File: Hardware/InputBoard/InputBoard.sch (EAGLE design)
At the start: 8 parts, among them IC1 LM358N

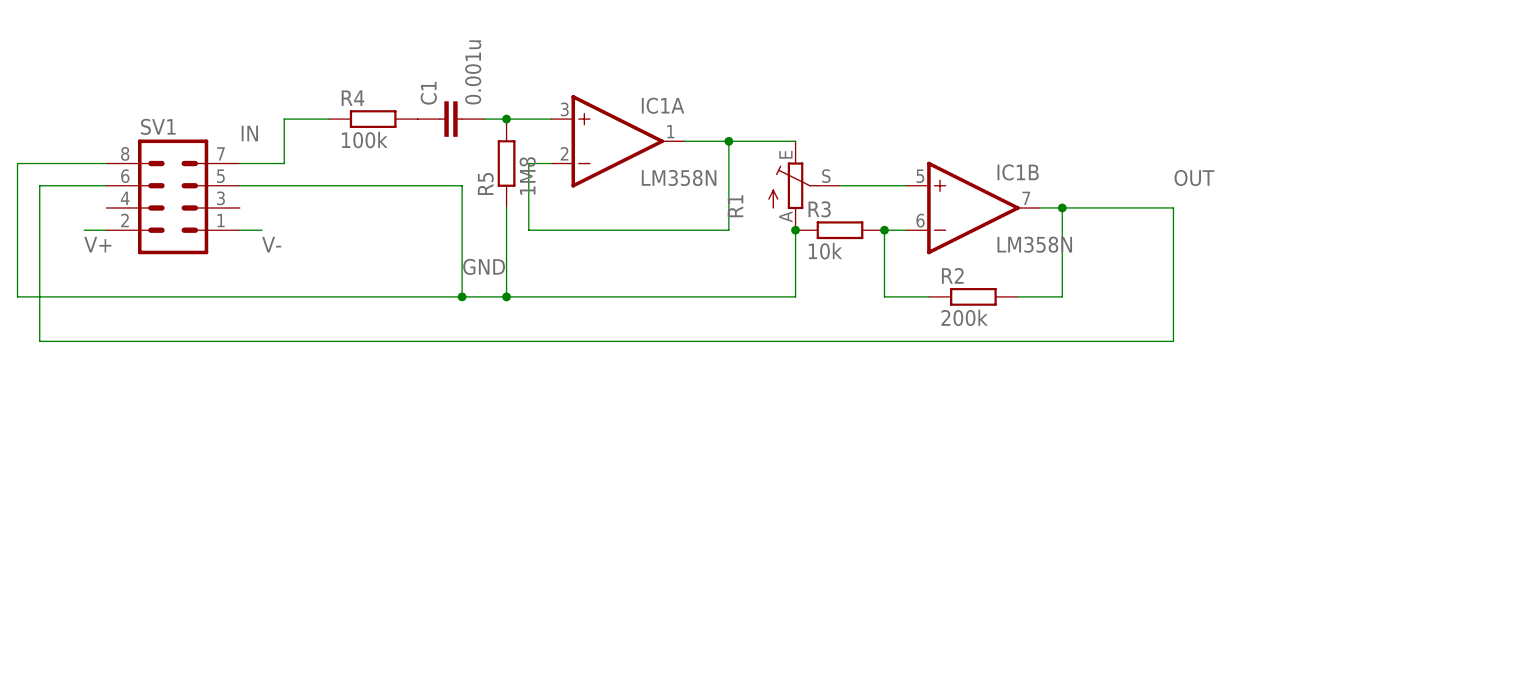
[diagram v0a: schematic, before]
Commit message: InputBoard überarbeitet, pinout bereitgestellt
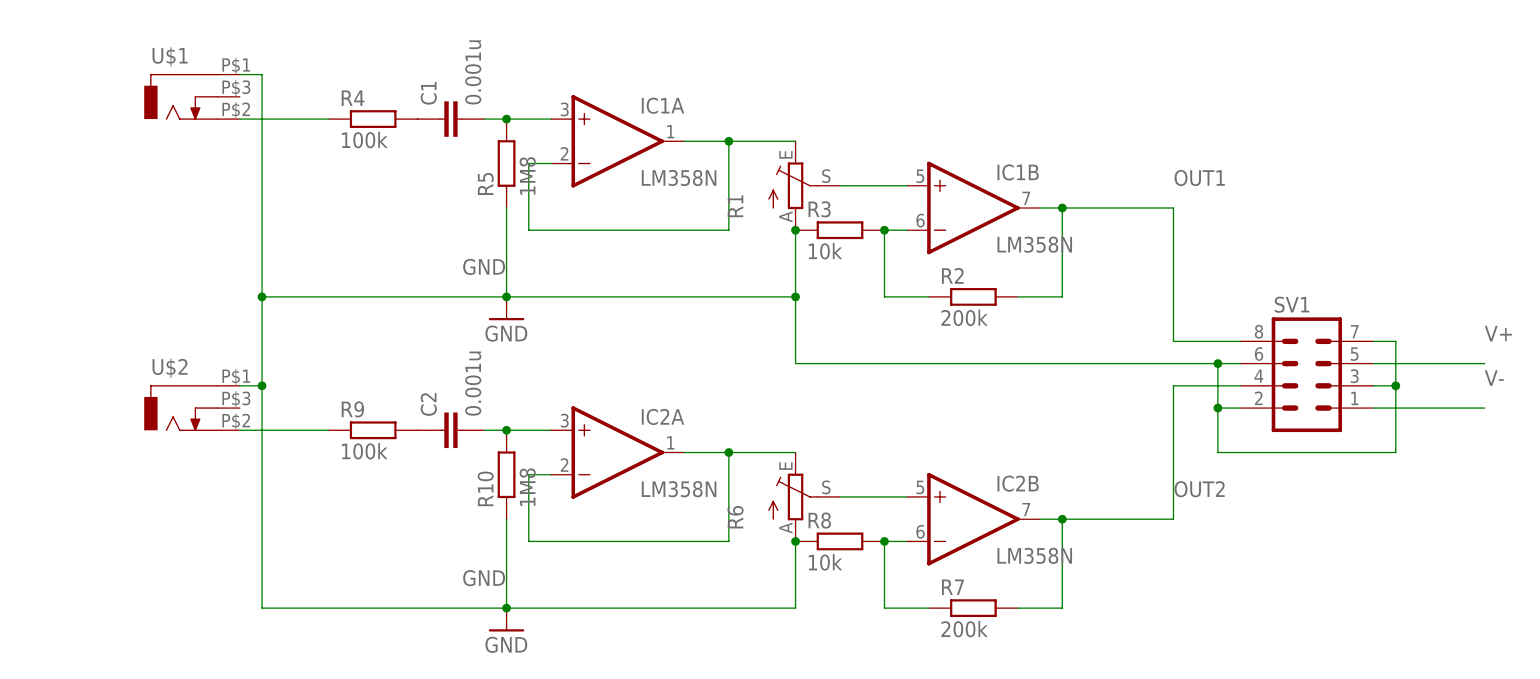
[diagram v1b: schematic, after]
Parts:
- added C2: 0.001u, rcl:C-EU050-025X075
- added IC2: LM358N, linear:LM358N
- added R10: 1M8, rcl:R-EU_0207/10
- added R6: (no value), pot:TRIM_EU-CIP20C-6MM
- added R7: 200k, rcl:R-EU_0207/10
- added R8: 10k, rcl:R-EU_0207/10
- added R9: 100k, rcl:R-EU_0207/10
- added U$1, U$2: (no value), EBS63P:EBS63P
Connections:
- removed net IN: R4.1, SV1.7
- removed net OUT: IC1B.OUT, R2.2, SV1.6
- new net N$10: C2.1, R9.2
- new net N$11: R9.1, U$2.3
- new net N$12: R4.1, U$1.3
- new net N$6: IC2A.-IN, IC2A.OUT, R6.E
- new net N$7: IC2B.+IN, R6.S
- new net N$8: IC2B.-IN, R7.1, R8.2
- new net N$9: C2.2, IC2A.+IN, R10.2
- new net OUT1: IC1B.OUT, R2.2, SV1.8
- new net OUT2: IC2B.OUT, R7.2, SV1.4
- net GND: now also R10.1, R6.A, R8.1, SV1.2, SV1.3, SV1.6, SV1.7, U$1.1, U$2.1; no longer SV1.5, SV1.8
- net V+: now also SV1.5; no longer SV1.2
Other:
- moved on the sheet: SV1

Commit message: Letzte Änderungen an Netzteil, OP und IP Board
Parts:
- added C3, C4: (no value), rcl:CPOL-EUE5-8.5
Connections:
- net GND: now also C3.-, C4.+
- net V+: now also C3.+
- net V-: now also C4.-
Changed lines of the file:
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@@
 <?xml version="1.0" encoding="utf-8"?>
 <!DOCTYPE eagle SYSTEM "eagle.dtd">
-<eagle version="9.4.1">
+<eagle version="9.4.0">
 <drawing>
 <settings>
@@
 <part name="U$1" library="EBS63P" deviceset="EBS63P" device=""/>
 <part name="U$2" library="EBS63P" deviceset="EBS63P" device=""/>
+<part name="C3" library="rcl" library_urn="urn:adsk.eagle:library:334" deviceset="CPOL-EU" device="E5-8.5" package3d_urn="urn:adsk.eagle:package:23374/1"/>
+<part name="C4" library="rcl" library_urn="urn:adsk.eagle:library:334" deviceset="CPOL-EU" device="E5-8.5" package3d_urn="urn:adsk.eagle:package:23374/1"/>
 </parts>
 <sheets>
@@
 <attribute name="NAME" x="0" y="36.83" size="1.778" layer="95"/>
 <attribute name="VALUE" x="0" y="26.67" size="1.778" layer="96"/>
+</instance>
+<instance part="C3" gate="G$1" x="142.24" y="45.72" smashed="yes">
+<attribute name="NAME" x="143.383" y="46.2026" size="1.778" layer="95"/>
+<attribute name="VALUE" x="143.383" y="41.1226" size="1.778" layer="96"/>
+</instance>
+<instance part="C4" gate="G$1" x="142.24" y="25.4" smashed="yes">
+<attribute name="NAME" x="143.383" y="25.8826" size="1.778" layer="95"/>
+<attribute name="VALUE" x="143.383" y="20.8026" size="1.778" layer="96"/>
 </instance>
 </instances>
@@
 <pinref part="U$1" gate="G$1" pin="1"/>
 <pinref part="U$2" gate="G$1" pin="1"/>
+<pinref part="C3" gate="G$1" pin="-"/>
+<junction x="142.24" y="40.64"/>
+<pinref part="C4" gate="G$1" pin="+"/>
+<junction x="142.24" y="27.94"/>
 </segment>
 </net>
@@
 <segment>
 <pinref part="SV1" gate="G$1" pin="5"/>
-<wire x1="139.7" y1="38.1" x2="152.4" y2="38.1" width="0.1524" layer="91"/>
+<wire x1="139.7" y1="38.1" x2="147.32" y2="38.1" width="0.1524" layer="91"/>
 <label x="152.4" y="40.64" size="1.778" layer="95"/>
+<pinref part="C3" gate="G$1" pin="+"/>
+<wire x1="147.32" y1="38.1" x2="152.4" y2="38.1" width="0.1524" layer="91"/>
+<wire x1="142.24" y1="48.26" x2="147.32" y2="48.26" width="0.1524" layer="91"/>
+<wire x1="147.32" y1="48.26" x2="147.32" y2="38.1" width="0.1524" layer="91"/>
+<junction x="147.32" y="38.1"/>
 </segment>
 </net>
@@
 <segment>
 <pinref part="SV1" gate="G$1" pin="1"/>
-<wire x1="139.7" y1="33.02" x2="152.4" y2="33.02" width="0.1524" layer="91"/>
+<wire x1="139.7" y1="33.02" x2="147.32" y2="33.02" width="0.1524" layer="91"/>
 <label x="152.4" y="35.56" size="1.778" layer="95"/>
-</segment>
-</net>
+<pinref part="C4" gate="G$1" pin="-"/>
+<wire x1="147.32" y1="33.02" x2="152.4" y2="33.02" width="0.1524" layer="91"/>
+<wire x1="142.24" y1="20.32" x2="147.32" y2="20.32" width="0.1524" layer="91"/>
+<wire x1="147.32" y1="20.32" x2="147.32" y2="33.02" width="0.1524" layer="91"/>
+<junction x="147.32" y="33.02"/>
+</segment>
+</net>
